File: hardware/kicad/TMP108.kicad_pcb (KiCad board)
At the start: 2 copper layers, 75 x 75 mm, 38 parts, among them J1 Screw_Terminal_01x08, J2 Screw_Terminal_01x08, J3 CAN, SW1 PRG, SW2 SCR, SW3 PRG-VALUE, U1 Teensy_3.2, U2 TMR-1211, U3 MCP2551-I-P

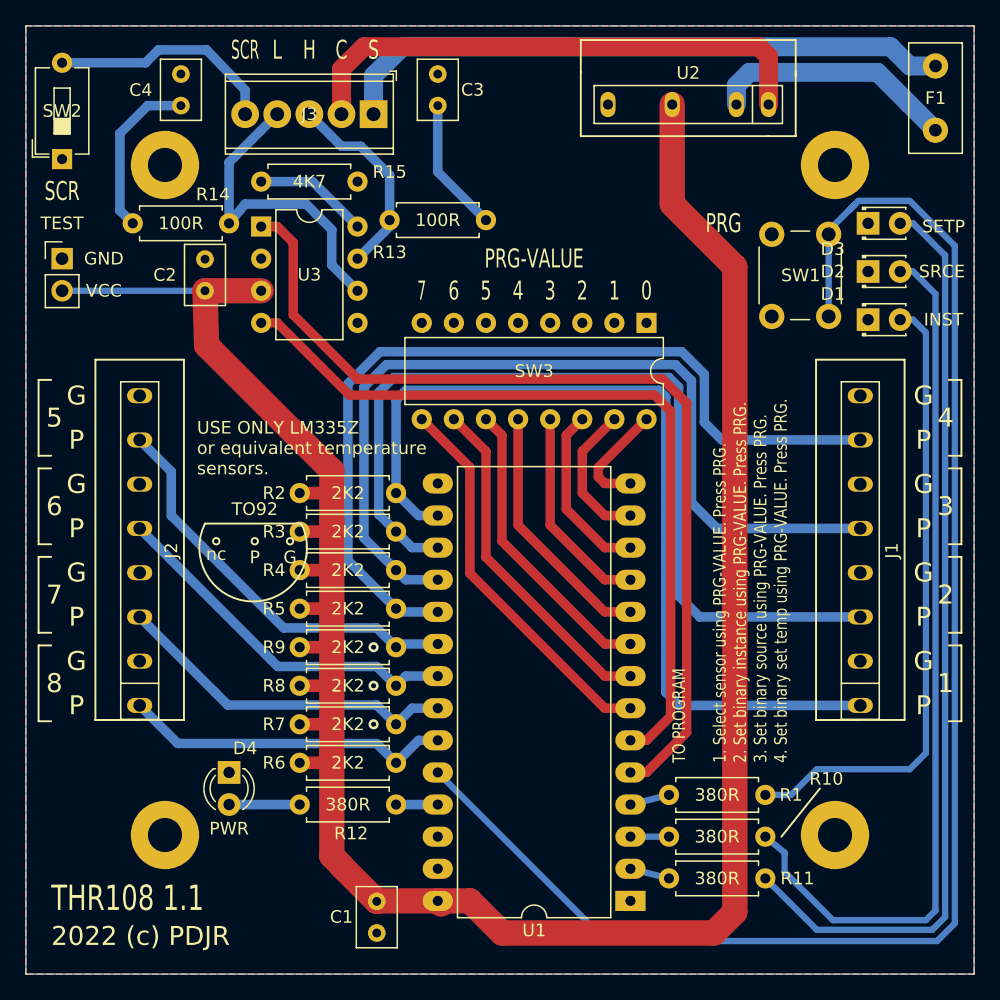
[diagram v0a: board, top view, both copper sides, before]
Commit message: Adjust PCB silk screen
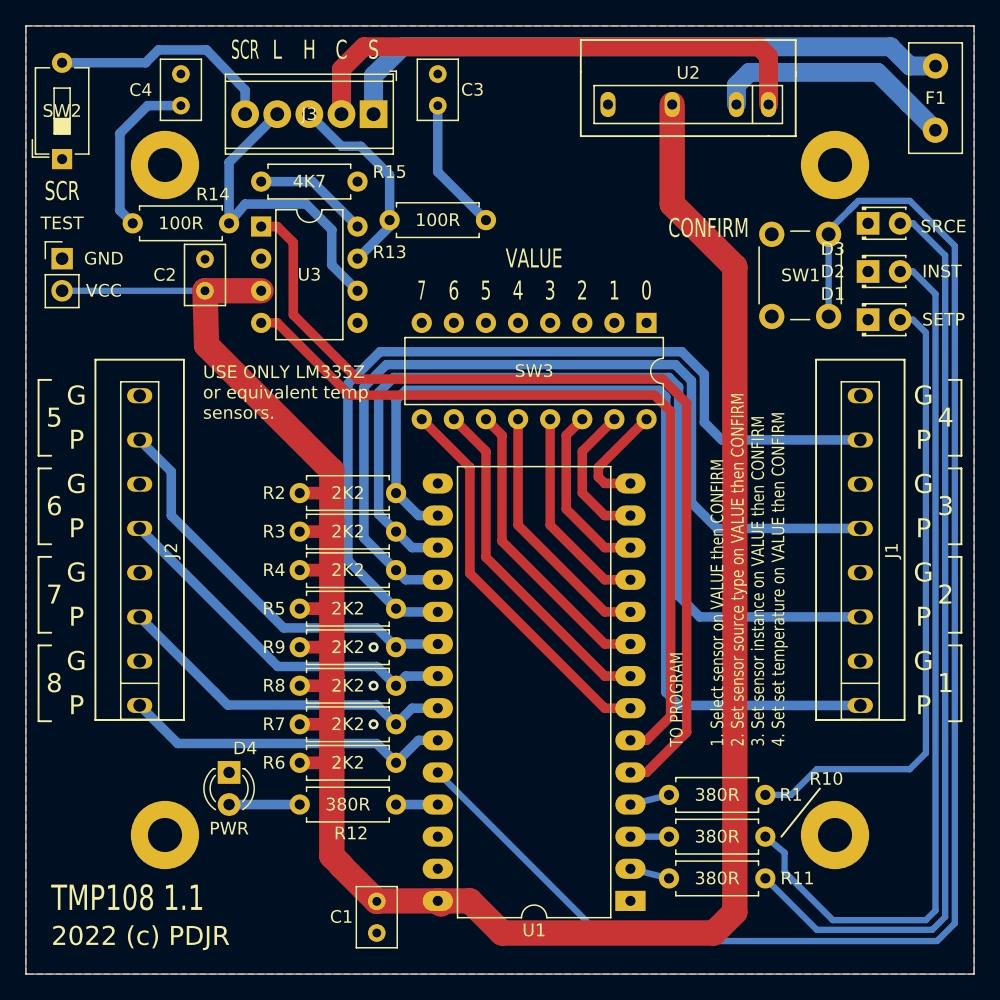
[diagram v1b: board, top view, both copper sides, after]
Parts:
- D1: value INST -> SETP
- D2: value SRCE -> INST
- D3: value SETP -> SRCE
- SW1: value PRG -> CONFIRM
- SW3: value PRG-VALUE -> VALUE
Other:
- board text added: "TMP108 1.1"
- board text added: "TO PROGRAM 1. Select sensor on VALUE then CONFIRM 2. Set sensor source type on VALUE then CONFIRM 3. Set sensor instance on VALUE then CONFIRM 4. Set set temperature on VALUE then CONFIRM"
- board text added: "USE ONLY LM335Z or equivalent temp sensors."
- board text removed: "THR108 1.1"
- board text removed: "TO PROGRAM 1. Select sensor using PRG-VALUE. Press PRG. 2. Set binary instance using PRG-VALUE. Press PRG. 3. Set binary source using PRG-VALUE. Press PRG. 4. Set binary set temp using PRG-VALUE. Press PRG."
- board text removed: "TO92"
- board text removed: "USE ONLY LM335Z or equivalent temperature sensors."
- board text removed: "nc"

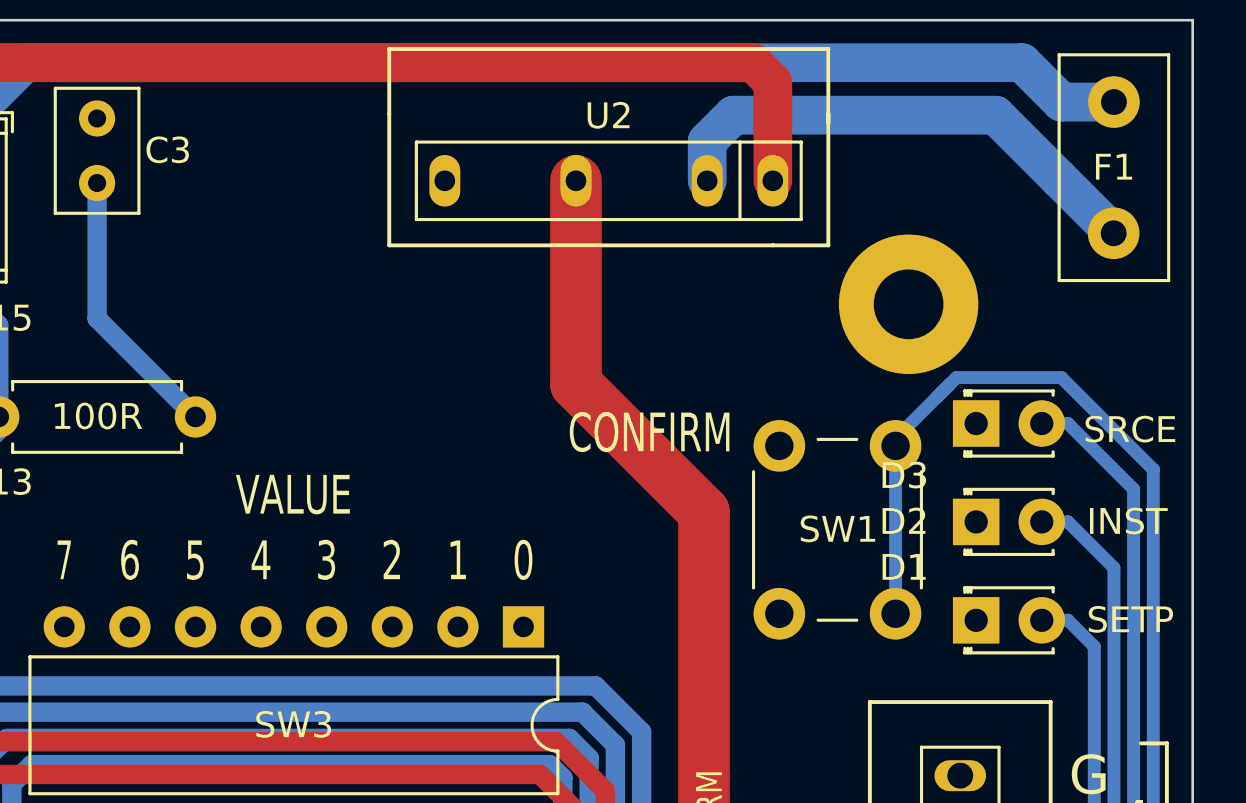
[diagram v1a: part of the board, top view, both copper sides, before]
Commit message: Add smoothing capacitor to PSU
1000uF capacitor across 5V output to manage instability in ADC reference voltage.
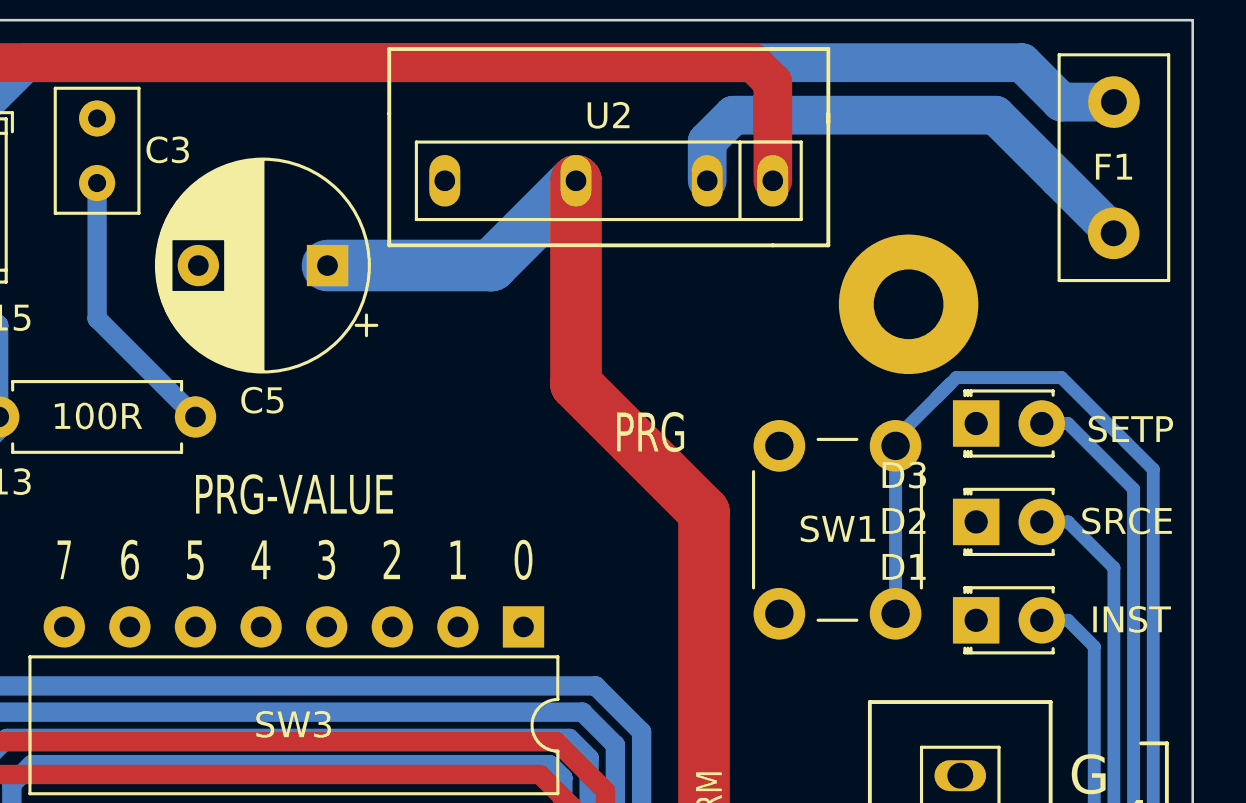
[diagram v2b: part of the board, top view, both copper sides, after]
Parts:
- added C5: CP, Capacitor_THT:CP_Radial_D8.0mm_P5.00mm, F.Cu at (177.5, 96.5)
- D1: value SETP -> INST
- D2: value INST -> SRCE
- D3: value SRCE -> SETP
- SW1: value CONFIRM -> PRG
- SW3: value VALUE -> PRG-VALUE
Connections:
- U1 pad 15: (no net) -> Net-(U1-Pad15)
- U1 pad 26: (no net) -> Net-(U1-Pad26)
- U3 pad 5: (no net) -> Net-(U3-Pad5)
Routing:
- net +5V: track 187.9 -> 198.9 mm

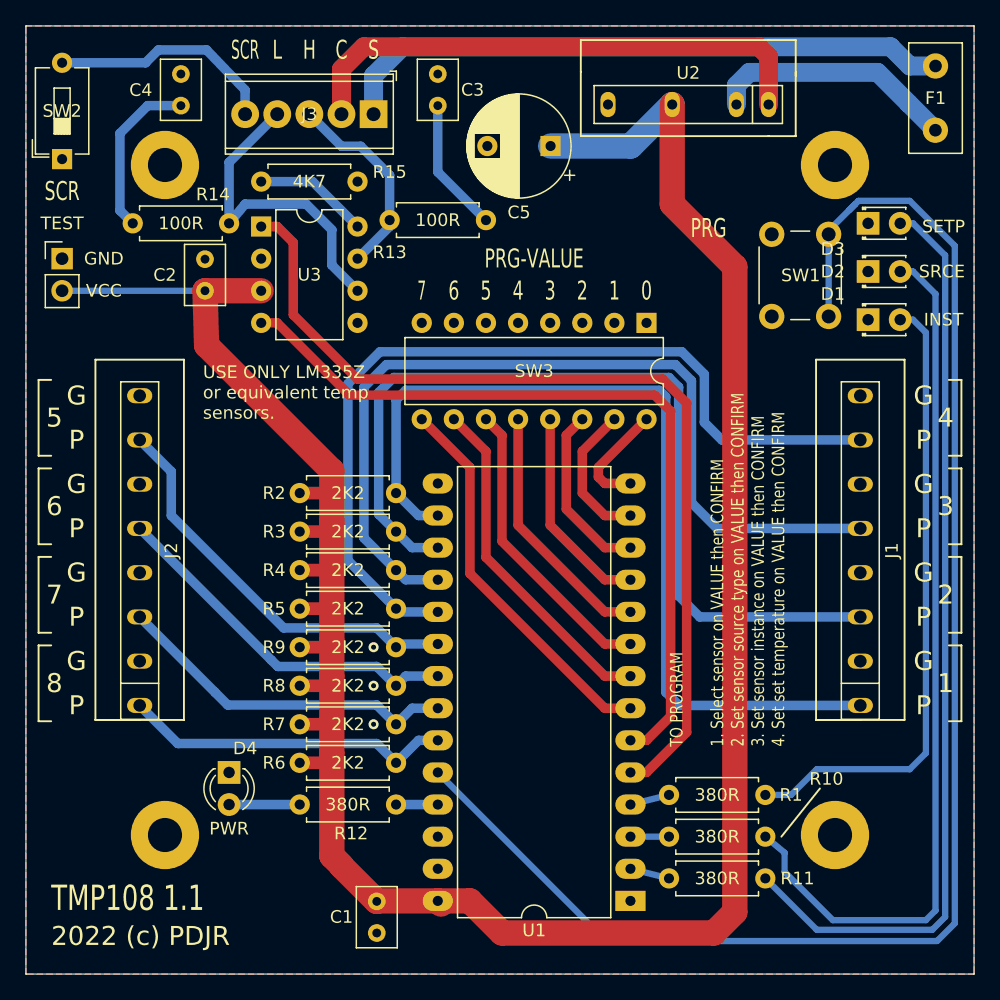
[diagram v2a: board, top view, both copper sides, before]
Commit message: Board tweaks
To avoid PCB fouling cover clips.
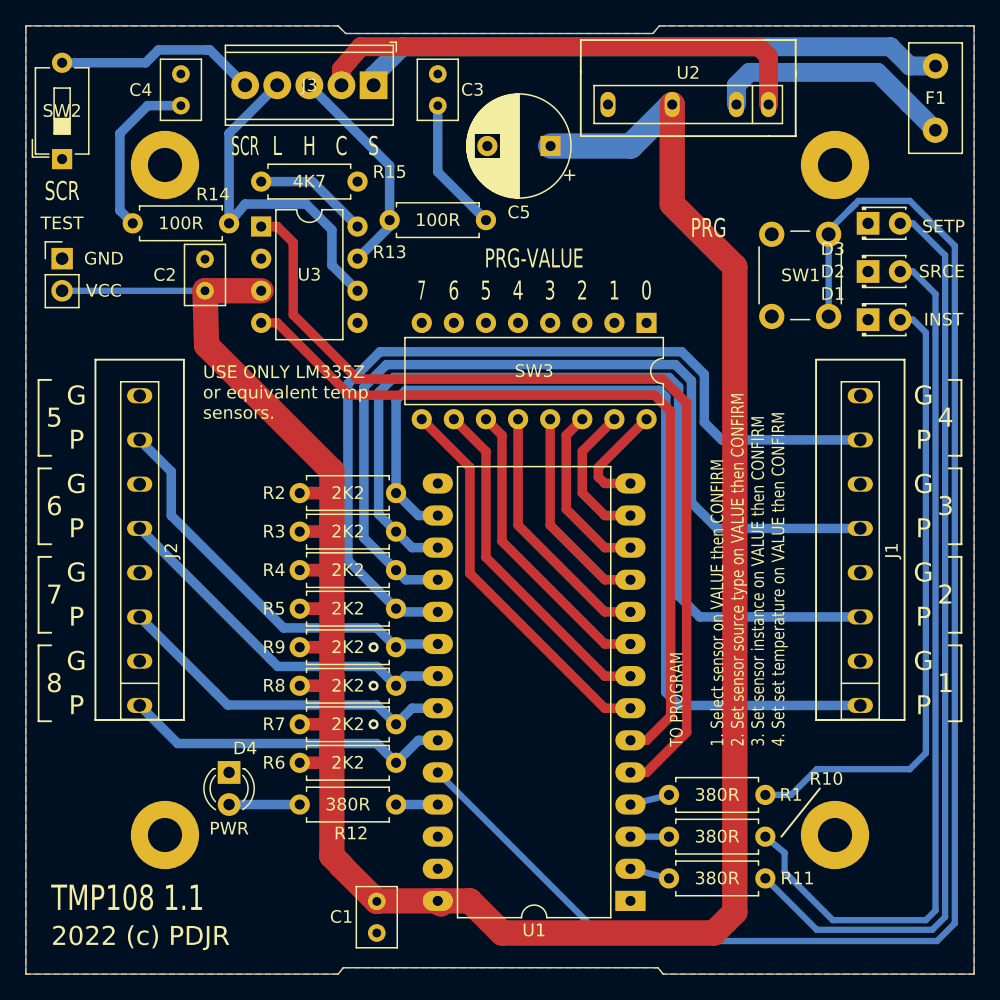
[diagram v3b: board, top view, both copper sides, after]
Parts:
- moved J3 2.29 mm to (163.5, 91.7)
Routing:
- net /NET_S: track 49.1 -> 46.1 mm
- net /NET_C: track 42.2 -> 39.3 mm
- net /CAN_L: track 25.6 -> 27.9 mm
- net /CAN_SCR: track 18.2 -> 16.1 mm
- net /CAN_H: track 16.0 -> 17.4 mm
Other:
- outline, holes or cut-outs redrawn

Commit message: Add cable tie holes to PCB
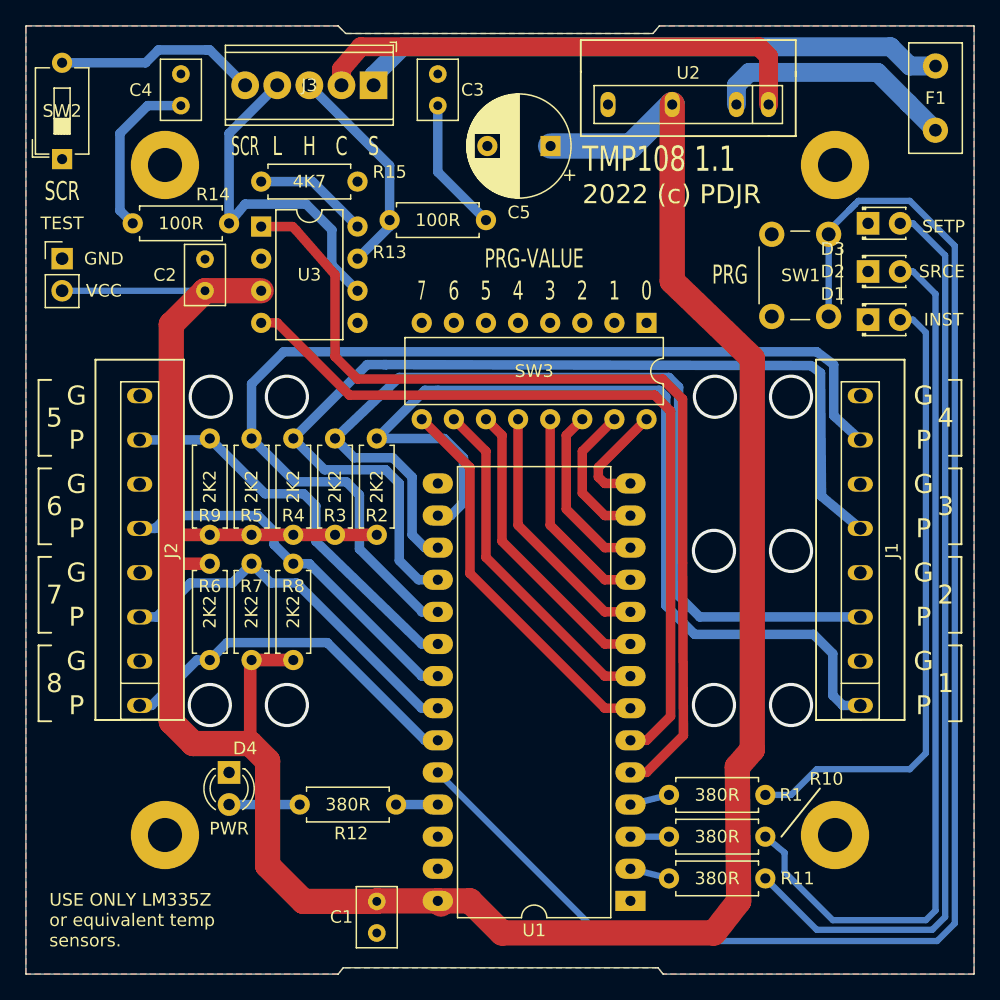
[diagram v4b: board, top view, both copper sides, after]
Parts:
- moved R9 22.1 mm to (150.5, 119.6), turned to 270 degrees
- moved R5 17.7 mm to (153.8, 119.6), turned to 270 degrees
- moved R7 17.1 mm to (153.8, 129.5), turned to 270 degrees
- moved R6 16.8 mm to (150.5, 137.2), turned to 90 degrees
- moved R4 13.2 mm to (157.2, 119.6), turned to 270 degrees
- moved R8 12.6 mm to (157.2, 129.5), turned to 270 degrees
- moved R3 8.81 mm to (160.5, 119.6), turned to 270 degrees
- moved R2 4.58 mm to (163.8, 119.6), turned to 270 degrees
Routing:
- net +5V: track 198.9 -> 215.6 mm
- net /SENSOR_T3: track 69.5 -> 81.6 mm
- net /SENSOR_T2: track 70.2 -> 78.0 mm
- net /SENSOR_T1: track 71.5 -> 75.4 mm
- net /SENSOR_T0: track 72.5 -> 75.3 mm
- net /SENSOR_T7: track 26.2 -> 28.8 mm
- net /SENSOR_T6: track 27.6 -> 30.1 mm
- net /SENSOR_T5: track 29.0 -> 29.9 mm
- net /SENSOR_T4: track 32.5 -> 31.9 mm
- net GND: vias 3 -> 10
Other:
- board text removed: "TO PROGRAM 1. Select sensor on VALUE then CONFIRM 2. Set sensor source type on VALUE then CONFIRM 3. Set sensor instance on VALUE then CONFIRM 4. Set set temperature on VALUE then CONFIRM"

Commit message: Add CAN terminator
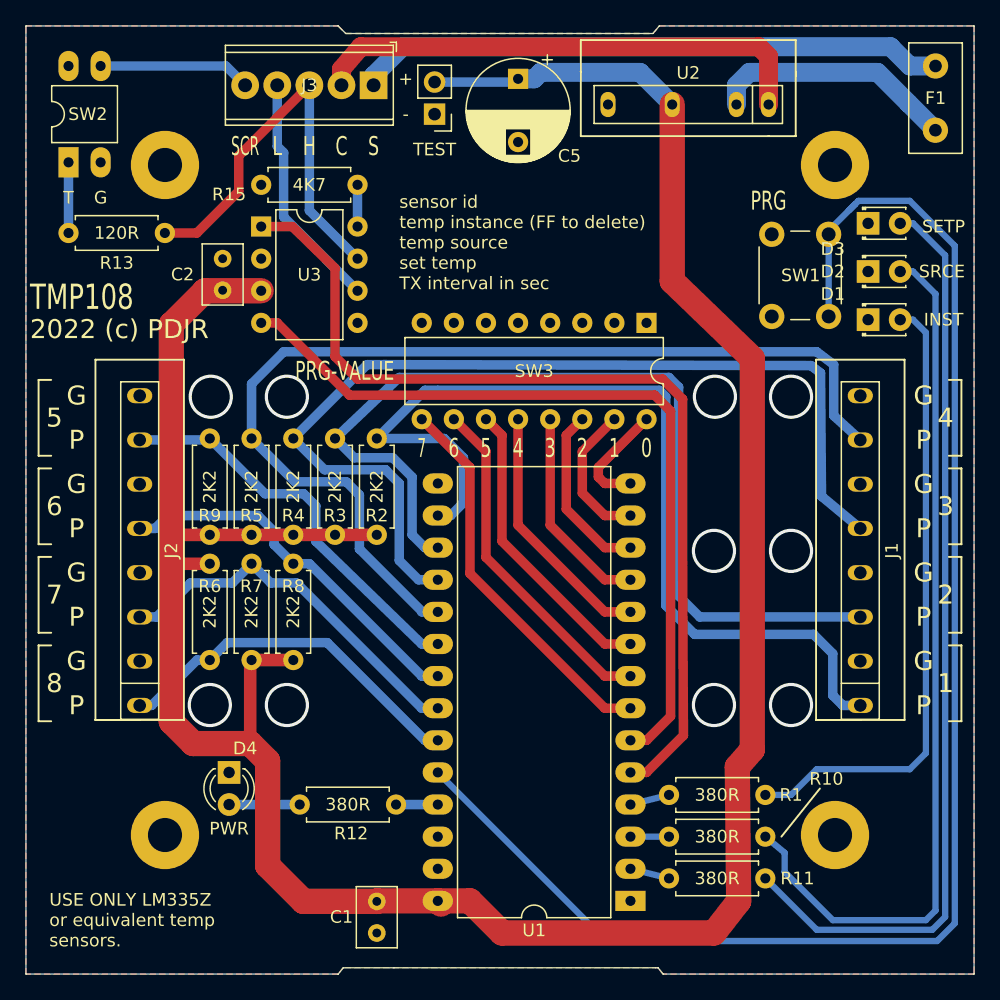
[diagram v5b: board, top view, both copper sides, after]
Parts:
- removed C3, C4: 560p, Capacitor_THT:C_Rect_L4.6mm_W3.0mm_P2.50mm_MKS02_FKP02
- removed R14: 100R, Resistor_THT:R_Axial_DIN0207_L6.3mm_D2.5mm_P7.62mm_Horizontal
- C5: value CP -> 1000uF
- R13: value 100R -> 120R
- SW2: value SCR -> BUS; footprint Button_Switch_THT:SW_DIP_SPSTx01_Slide_6.7x4.1mm_W7.62mm_P2.54mm_LowProfile -> Package_DIP:DIP-4_W7.62mm_LongPads
- moved TEST 31.6 mm to (168.3, 94.0), turned to 180 degrees
- moved R13 17.8 mm to (147.0, 103.4), turned to 180 degrees
- moved R15 7.62 mm to (154.6, 99.6), turned to 0 degrees
- moved C5 5.90 mm to (174.9, 91.2), turned to 270 degrees
- moved C2 1.40 mm to (151.6, 107.9)
- moved SW2 0.57 mm to (139.4, 97.8)
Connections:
- R13 pad 2: Net-(C3-Pad2) -> /TERM_A
- SW2 pad 1: GND -> /TERM_A
- SW2 pad 2: /CAN_SCR -> GND
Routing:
- net /CAN_H: track 17.4 -> 33.2 mm
- net Net-(C4-Pad2): track 13.3 -> 0.00 mm
- net Net-(C3-Pad2): track 10.6 -> 0.00 mm
- net /CAN_L: track 27.9 -> 18.9 mm
- net /TERM_A: track 0.00 -> 5.59 mm
- net Net-(R15-Pad2): track 9.09 -> 3.56 mm
- net /CAN_SCR: track 16.1 -> 12.1 mm
- net +5V: track 215.6 -> 213.5 mm
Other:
- board text added: "+"
- board text added: "-"
- board text added: "T"
- board text added: "TMP108"
- board text added: "sensor id temp instance (FF to delete) temp source set temp TX interval in sec"
- board text removed: "GND"
- board text removed: "TMP108 1.1"
- board text removed: "VCC"

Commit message: Routing
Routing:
- net /CAN_L: track 18.9 -> 38.0 mm
